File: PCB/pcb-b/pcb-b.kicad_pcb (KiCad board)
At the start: 2 copper layers, 94.1 x 41.1 mm, 79 parts, among them J1 Conn_02x05_Counter_Clockwise, J2 Conn_02x05_Counter_Clockwise, K1 HK19F-DCxxV-SHC, Q1 BC817, Q11 TPCA8120,L1Q, Q13 TPCA8120,L1Q, Q14 BC817, Q15 BC817, Q19 BC817, Q2 BC817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

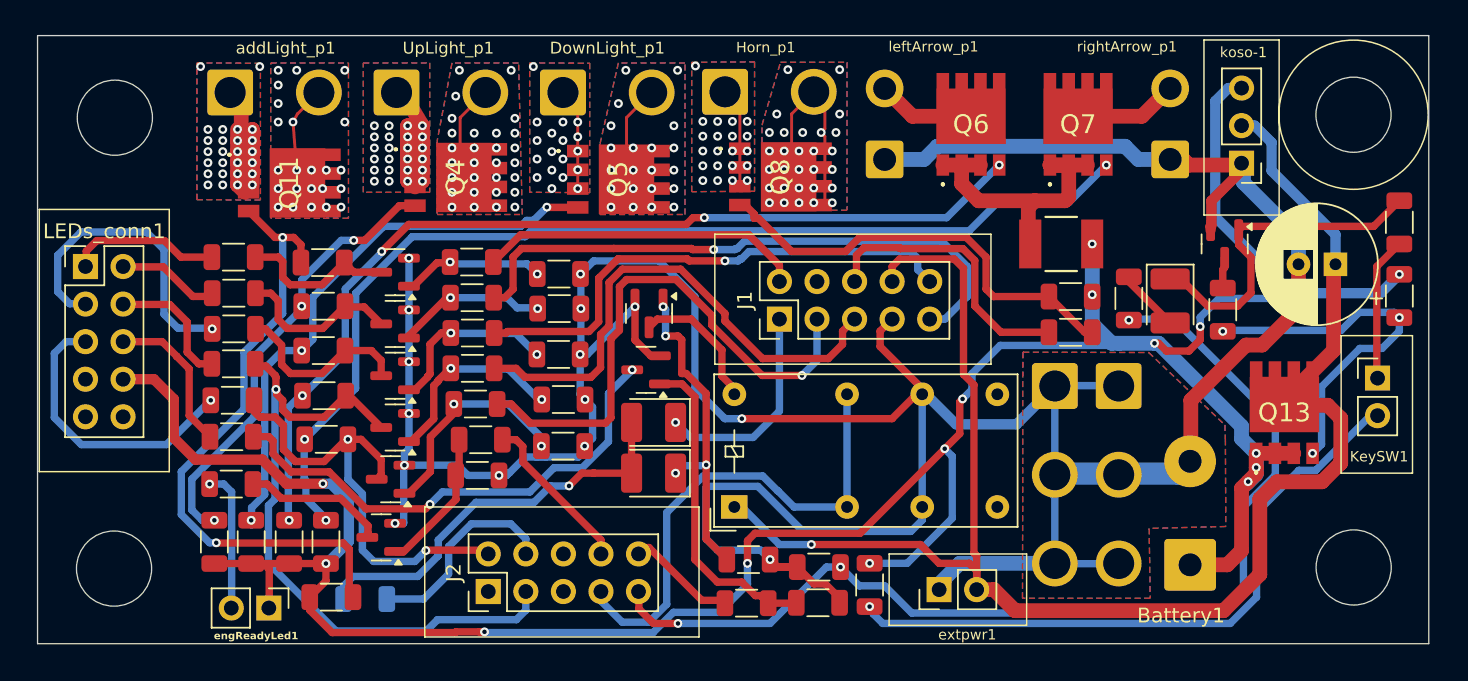
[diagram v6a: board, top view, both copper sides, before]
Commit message: PCBs sizes adjustment to be mounted as totem
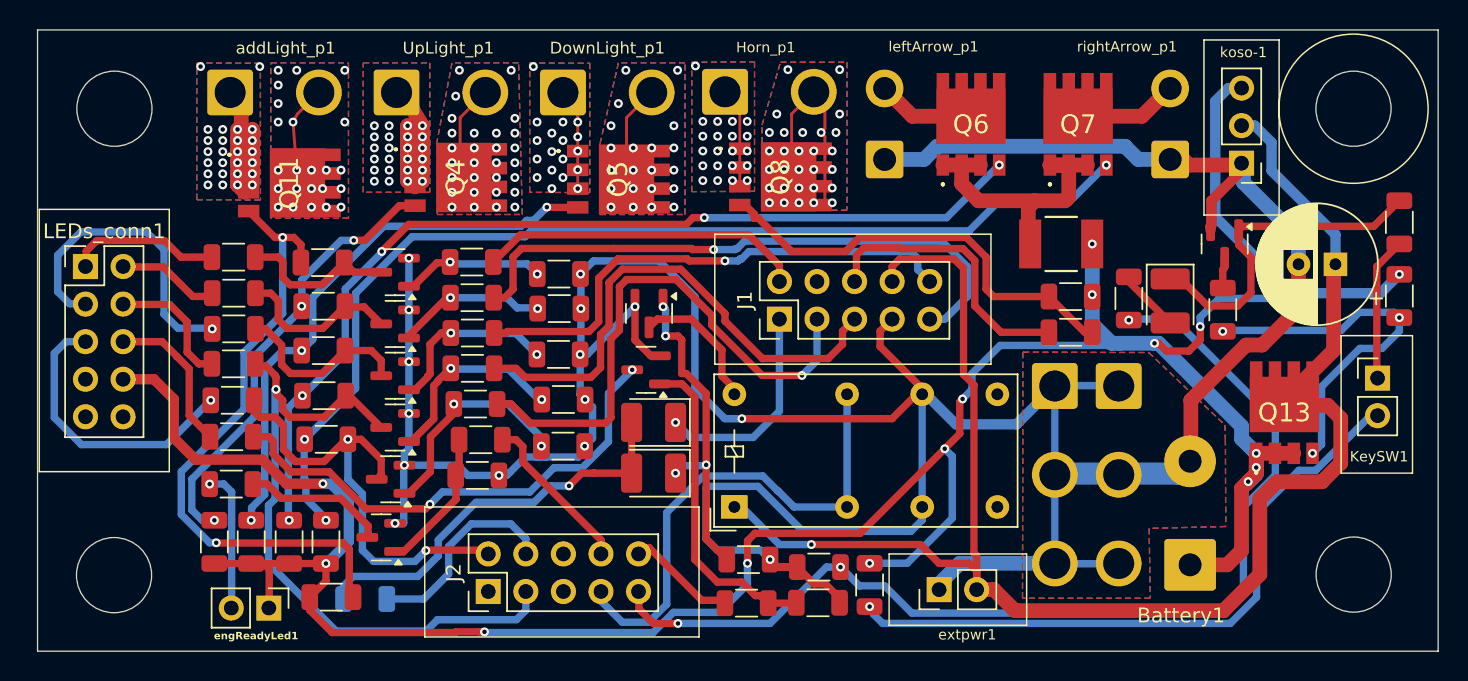
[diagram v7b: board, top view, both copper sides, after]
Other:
- board size 94.1 x 41.1 mm -> 94.7 x 42 mm
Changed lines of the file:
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@@
 	)
 	(gr_circle
-		(center 191.346112 75.6054)
-		(end 196.389797 75.6054)
+		(center 191.346112 75.199)
+		(end 196.389797 75.199)
 		(stroke
 			(width 0.1)
@@
 	)
 	(gr_circle
-		(center 191.346179 75.6054)
-		(end 193.886179 75.594835)
-		(stroke
-			(width 0.05)
-			(type solid)
-		)
-		(fill no)
-		(layer "Edge.Cuts")
-	)
-	(gr_circle
-		(center 107.551621 106.2886)
-		(end 110.091621 106.278035)
-		(stroke
-			(width 0.05)
-			(type solid)
-		)
-		(fill no)
-		(layer "Edge.Cuts")
-	)
-	(gr_circle
-		(center 107.606382 75.806315)
-		(end 110.146382 75.79575)
-		(stroke
-			(width 0.05)
-			(type solid)
-		)
-		(fill no)
-		(layer "Edge.Cuts")
-	)
-	(gr_circle
-		(center 191.357182 106.2124)
-		(end 193.897182 106.201835)
+		(center 191.346179 75.199)
+		(end 193.886179 75.188435)
+		(stroke
+			(width 0.05)
+			(type solid)
+		)
+		(fill no)
+		(layer "Edge.Cuts")
+	)
+	(gr_circle
+		(center 107.551621 106.731315)
+		(end 110.091621 106.72075)
+		(stroke
+			(width 0.05)
+			(type solid)
+		)
+		(fill no)
+		(layer "Edge.Cuts")
+	)
+	(gr_circle
+		(center 107.577 75.199022)
+		(end 110.117 75.188457)
+		(stroke
+			(width 0.05)
+			(type solid)
+		)
+		(fill no)
+		(layer "Edge.Cuts")
+	)
+	(gr_circle
+		(center 191.357182 106.695)
+		(end 193.897182 106.684435)
 		(stroke
 			(width 0.05)
@@
 	)
 	(gr_rect
-		(start 102.3792 70.255)
-		(end 196.4326 111.3662)
-		(stroke
-			(width 0.05)
-			(type solid)
-		)
-		(fill no)
-		(layer "Edge.Cuts")
-	)
-	(gr_circle
-		(center 107.551554 106.2886)
-		(end 112.181755 108.2886)
+		(start 102.3792 69.874)
+		(end 197.0676 111.8742)
+		(stroke
+			(width 0.05)
+			(type solid)
+		)
+		(fill no)
+		(layer "Edge.Cuts")
+	)
+	(gr_circle
+		(center 107.551554 106.731315)
+		(end 112.181755 108.731315)
 		(stroke
 			(width 0.1)
@@
 	)
 	(gr_circle
-		(center 107.606315 75.806315)
-		(end 112.236516 77.806315)
+		(center 107.576933 75.199022)
+		(end 112.207134 77.199022)
 		(stroke
 			(width 0.1)
@@
 	)
 	(gr_circle
-		(center 191.357115 106.2124)
-		(end 195.987316 108.2124)
+		(center 191.357115 106.695)
+		(end 195.987316 108.695)
 		(stroke
 			(width 0.1)
@@
 		(layer "B.Mask")
 		(pts
-			(xy 107.606382 75.806315) (xy 107.551621 106.2886)
+			(xy 107.577 75.199022) (xy 107.551621 106.731315)
 		)
 		(height 10.667932)
@@
 			(keep_text_aligned yes)
 		)
-		(gr_text "30,4823 mm"
-			(at 95.761088 91.026227 89.89706717)
+		(gr_text "31,5323 mm"
+			(at 95.746381 90.955657 89.95388326)
 			(layer "B.Mask")
 			(effects
@@
 		(layer "B.Mask")
 		(pts
-			(xy 102.3792 70.255) (xy 196.4326 70.255)
+			(xy 102.3792 69.874) (xy 197.0676 69.874)
 		)
 		(height -4.738)
@@
 			(keep_text_aligned yes)
 		)
-		(gr_text "94,0534 mm"
-			(at 149.4059 64.367 0)
+		(gr_text "94,6884 mm"
+			(at 149.7234 63.986 0)
 			(layer "B.Mask")
 			(effects
@@
 		(layer "B.Mask")
 		(pts
-			(xy 196.4326 111.3662) (xy 196.4326 70.255)
+			(xy 197.0676 111.8742) (xy 197.0676 69.874)
 		)
 		(height 6.593)
@@
 			(keep_text_aligned yes)
 		)
-		(gr_text "41,1112 mm"
-			(at 201.8756 90.8106 90)
-			(layer "B.Mask")
-			(effects
+		(gr_text "42,0002 mm"
+			(at 202.5106 90.8741 90)
+			(layer "B.Mask")
+			(effects

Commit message: Fix: horn still usable also when the mb is off
Horn is enabled by tempPower, now
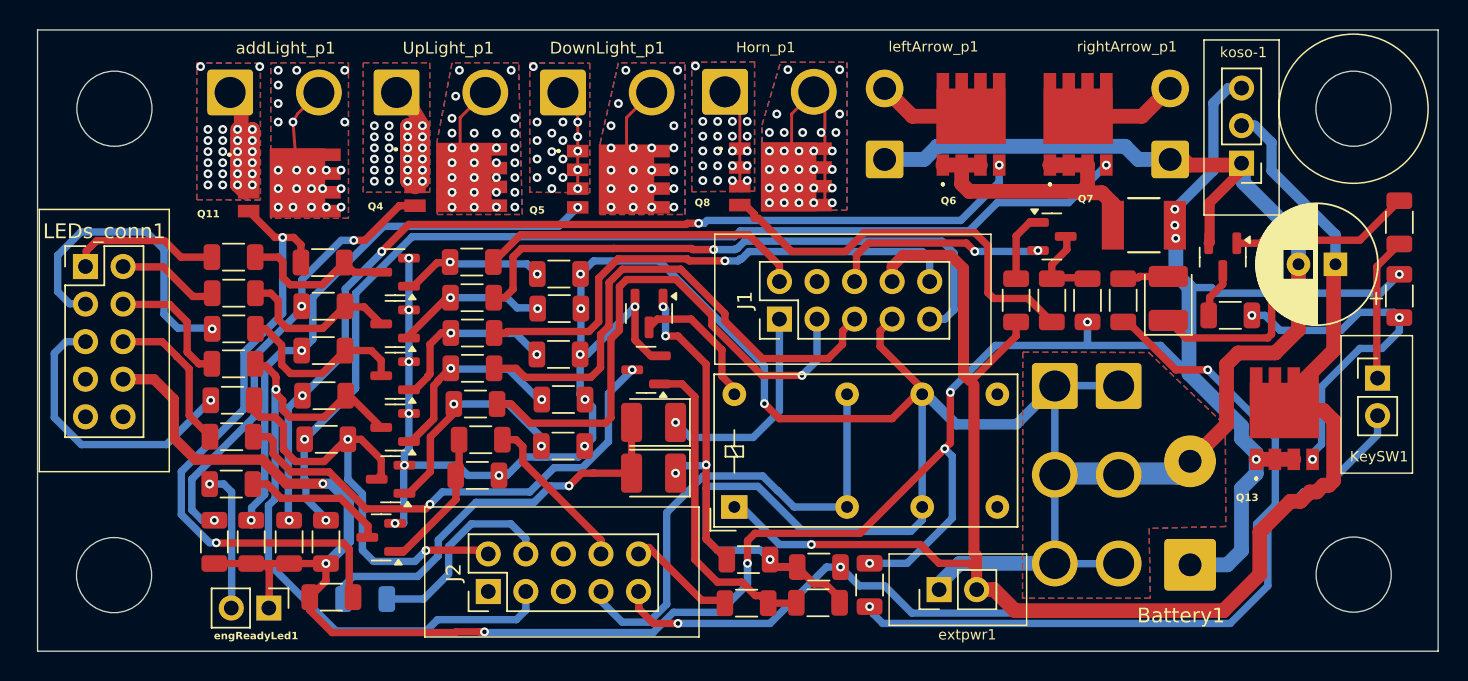
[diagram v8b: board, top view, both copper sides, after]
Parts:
- added Q10: BC817, Package_TO_SOT_SMD:SOT-23, F.Cu at (170.9, 83.8)
- added RA23: 20K, Resistor_SMD:R_1206_3216Metric, F.Cu at (168.5, 88.2)
- moved F2 5.73 mm to (177.2, 83.1)
- moved RA7 2.50 mm to (170.9, 88.2), turned to 90 degrees
- moved RA42 1.17 mm to (173.4, 88.2), turned to -90 degrees
- moved Q9 0.90 mm to (182.5, 85.2)
- moved R3 0.63 mm to (183.0, 89.2), turned to 0 degrees
- moved Q13 0.41 mm to (186.7, 96.2)
- moved R5 0.40 mm to (175.8, 88.2)
- moved D1 0.21 mm to (178.8, 88.0), turned to 90 degrees
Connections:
- RA42 pad 1: Net-(Q8-G) -> Net-(Q10-C)
- RA7 pad 2: c_horn -> Net-(Q10-C)
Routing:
- net +12V: track 193.1 -> 184.4 mm, vias 15 -> 13
- net Net-(Q10-C): track 0.00 -> 5.77 mm
- net Net-(Q10-B): track 0.00 -> 4.74 mm
- net tempPower: track 111.3 -> 115.9 mm
- net c_horn: track 19.2 -> 14.7 mm, vias 0 -> 2
- net Net-(D1-K): track 22.9 -> 26.3 mm
- net Net-(Q8-G): track 29.6 -> 27.4 mm
- net Net-(Q9-C): track 2.10 -> 3.39 mm
- net Net-(Q6-S_1): track 20.8 -> 21.9 mm
- net Net-(Q13-G): track 25.1 -> 23.9 mm
- net Net-(D1-A): track 4.27 -> 3.30 mm
- net GND: track 241.6 -> 240.7 mm
- net o_upLight: track 40.9 -> 40.1 mm
- net Net-(Q6-G): track 65.1 -> 65.7 mm
- net Net-(D2-K): track 22.3 -> 21.7 mm
